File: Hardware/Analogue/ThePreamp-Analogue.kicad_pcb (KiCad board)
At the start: 2 copper layers, 247 x 65 mm, 39 parts, among them IC1 ULN2803CDWR, J1 To preamp, J14 Conn_01x03_Pin, J15 PinSocket10x1, J2 From preamp, J3 Digital In, J4 Digital Pass Through, J5 Power In, J6 Power Out, J7 ADS1115, K1 Input 1, K2 Input 2, K3 Input 3, K4 Input 4, K5 Output Mute, K6 Trigger 1, K7 Trigger 2, K8 Input 5 (opt.), U1 MCP23008-E_SO

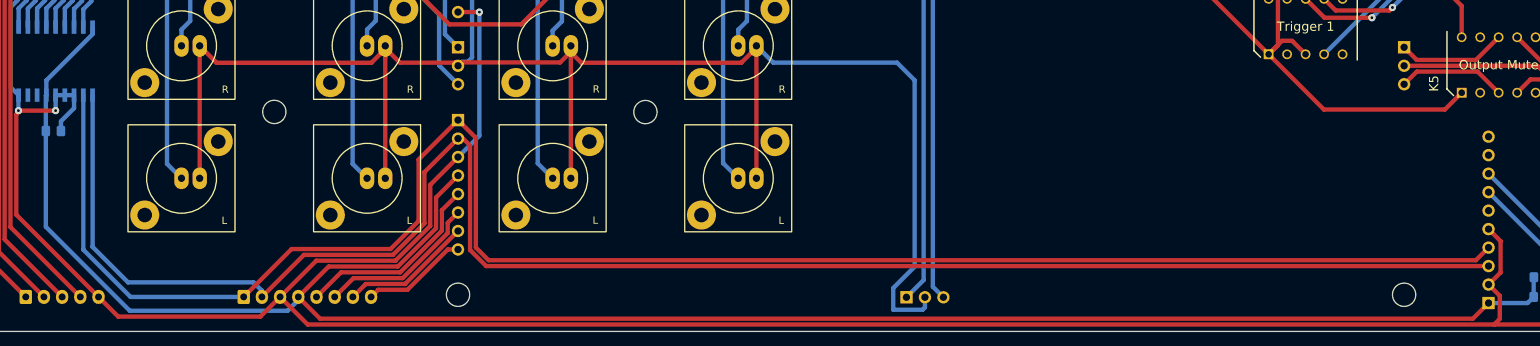
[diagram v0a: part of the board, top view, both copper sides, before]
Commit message: 16 pin IDC connector added for digital control input (GND interleaved)
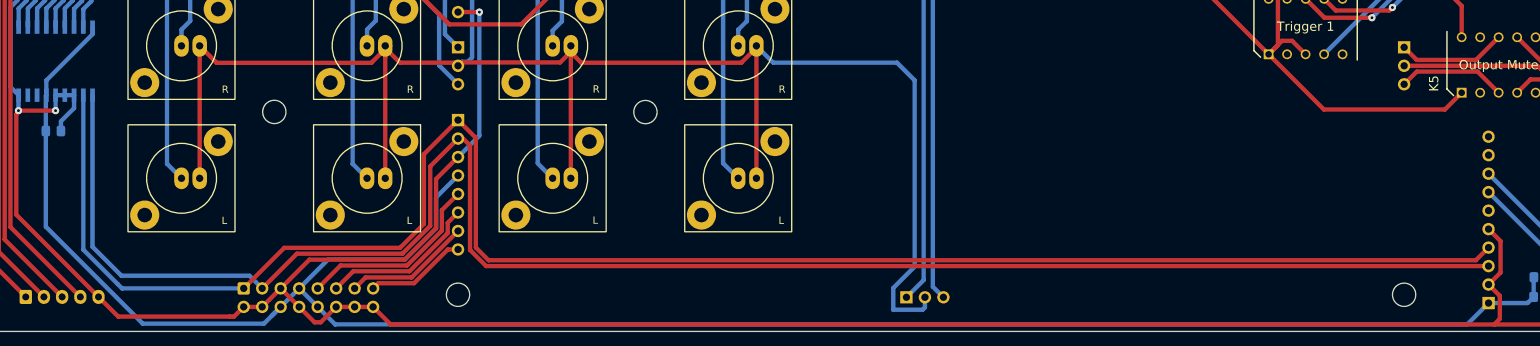
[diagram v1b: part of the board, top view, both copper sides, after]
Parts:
- J15: value PinSocket10x1 -> Switch & trigger outputs and analog inputs
- J3: footprint Connector_JST:JST_XH_B8B-XH-A_1x08_P2.50mm_Vertical -> Connector_IDC:IDC-Header_2x08_P2.54mm_Vertical
- moved J3 1.17 mm to (45.1, 135.9), turned to -90 degrees
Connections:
- J3 pad 2: I2C:SCL -> GND
- J3 pad 3: GND -> I2C:SCL
- J3 pad 4: +3.3V -> GND
- J3 pad 5: SPI:SCK -> GND
- J3 pad 6: SPI:MISO -> +3.3V
- J3 pad 7: SPI:MOSI -> +3.3V
- J3 pad 8: SPI:SS -> GND
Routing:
- net +3.3V: track 277.3 -> 280.9 mm
- net I2C:SCL: track 245.9 -> 243.9 mm
- net GND: track 400.6 -> 402.3 mm
- net SPI:SS: track 14.7 -> 13.9 mm
- net SPI:MOSI: track 18.2 -> 17.5 mm
- net SPI:MISO: track 22.6 -> 21.9 mm
- net SPI:SCK: track 27.0 -> 26.3 mm

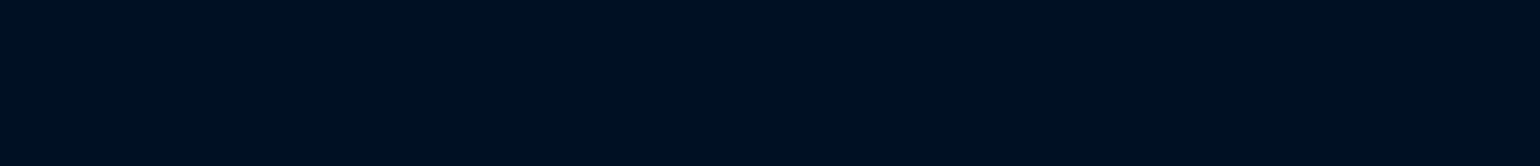
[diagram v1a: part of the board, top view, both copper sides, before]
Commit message: Digital connector (IDC 16) aligned on controller and analog board
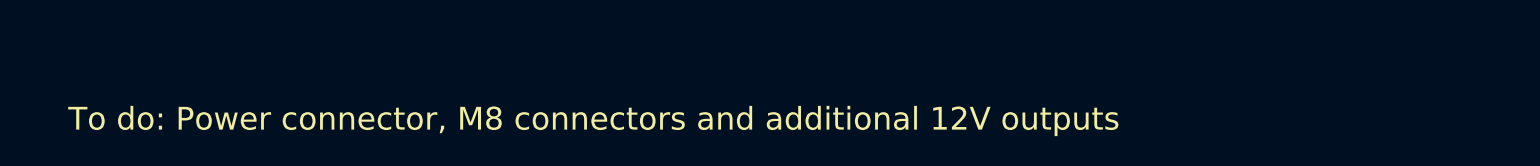
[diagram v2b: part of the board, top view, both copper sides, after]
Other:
- board text added: "To do: Power connector, M8 connectors and additional 12V outputs"
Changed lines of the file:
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@@
     (effects (font (size 1 1) (thickness 0.15)) (justify left bottom mirror))
+  )
+  (gr_text "To do: Power connector, M8 connectors and additional 12V outputs" (at 70.82 153.93) (layer "F.SilkS")
+    (effects (font (size 2 2) (thickness 0.15)) (justify left bottom))
   )
   (gr_text "R" (at 42.11 109.12) (layer "F.SilkS")

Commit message: Added optional M8 connectors for switches, 12V triggers and analog measurements
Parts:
- added J10: Conn_01x04, Connector_M8:M8 4 pin, F.Cu at (268.0, 129.2)
- added J11: Conn_01x03, Connector_M8:M8 3 pin, F.Cu at (285.4, 129.2)
- added J8: Conn_01x04, Connector_M8:M8 4 pin, F.Cu at (267.9, 99.3)
- added J9: Conn_01x03, Connector_M8:M8 3 pin, F.Cu at (285.3, 99.4)
- moved G*** 40.4 mm to (275.8, 87.0)
- moved C1 1.21 mm to (19.0, 113.0)
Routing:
- net GND: track 402.3 -> 481.1 mm
- net Trigger 2 12V out: track 81.5 -> 122.5 mm
- net Trigger 1 12V out: track 70.8 -> 108.1 mm
- net Switch 2 pin 1: track 87.2 -> 115.0 mm
- net Switch 1 pin 1: track 73.1 -> 98.1 mm
- net Switch 2 pin 2: track 88.5 -> 111.2 mm
- net A0: track 71.1 -> 91.9 mm
- net Switch 1 pin 2: track 70.9 -> 91.6 mm
- net A1: track 64.8 -> 84.3 mm
- net +12V: track 300.9 -> 299.5 mm
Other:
- board size 247 x 65 mm -> 285 x 65 mm
- board text added: "To do: Power connector"
- board text added: "v1.1 2024-03"
- board text removed: "To do: Power connector, M8 connectors and additional 12V outputs"
- board text removed: "v1.1 2024-02"

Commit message: Changed power connectors
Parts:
- removed the J5 at (15.2, 137.0)
- removed the REF** at (49.3, 111.6)
- removed the REF** at (100.3, 111.6)
- added J7: Audio Power In, THEPREAMP_POWER_CON:TBP01R2-508-03BK (VERT), B.Cu at (13.0, 137.1)
- added J8: Relay Power In, THEPREAMP_POWER_CON:TBP01R2-508-02BK (VERT), B.Cu at (30.8, 137.1)
- J9: renamed from J7; moved to F.Cu
- moved K8 98.8 mm to (280.8, 120.6), turned to 180 degrees
- moved K7 95.7 mm to (280.8, 90.9), turned to 180 degrees
- moved G*** 50.8 mm to (225.0, 87.4)
- moved C1 11.5 mm to (26.8, 104.6), turned to -90 degrees
- moved J10 6.87 mm to (258.3, 120.5)
- turned J9 to 180 degrees
- renumbered J15 to J10, J8 to J11, J9 to J12, J10 to J13, J11 to J14, J14 to J5, K8 to K2, K2 to K3, K3 to K4, K4 to K5, K5 to K6, K6 to K7, K7 to K8, R3 to R1, R4 to R2, RCA9 to RCA5, RCA5 to RCA6, RCA6 to RCA7, RCA7 to RCA8, RCA8 to RCA9
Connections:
- K7 pad 7: Switch 1 pin 2 -> Switch 1 pin 1
- K7 pad 8: Switch 1 pin 1 -> Switch 1 pin 2
- K8 pad 7: Switch 2 pin 2 -> Switch 2 pin 1
- K8 pad 8: Switch 2 pin 1 -> Switch 2 pin 2
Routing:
- net +12V: track 299.5 -> 466.0 mm, vias 1 -> 3
- net RELAY7: track 173.4 -> 305.8 mm, vias 1 -> 0
- net RELAY6: track 178.8 -> 263.8 mm
- net Trigger 2 12V out: track 122.5 -> 39.9 mm
- net Switch 2 pin 2: track 111.2 -> 30.7 mm
- net Switch 2 pin 1: track 115.0 -> 42.6 mm
- net Switch 1 pin 2: track 91.6 -> 29.2 mm, vias 1 -> 0
- net Trigger 1 12V out: track 108.1 -> 46.7 mm
- net Switch 1 pin 1: track 98.1 -> 38.3 mm, vias 1 -> 0
- net +3.3V: track 280.9 -> 286.6 mm
- net -15V: track 113.1 -> 117.5 mm
- net GND: track 481.1 -> 476.9 mm
- net A0: track 91.9 -> 93.2 mm
- net +15V: track 112.9 -> 112.0 mm
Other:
- board text removed: "G_A"
- board text removed: "To do: Power connector"

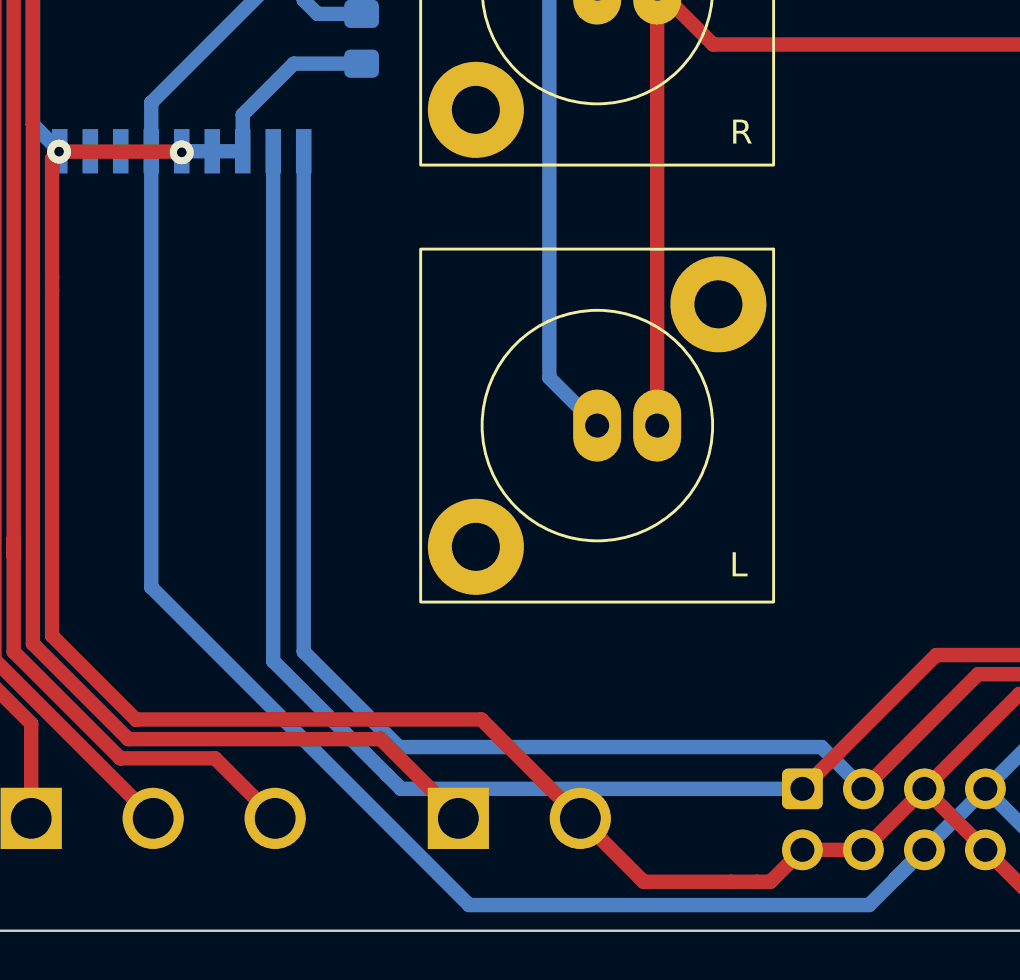
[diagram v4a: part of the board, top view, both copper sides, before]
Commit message: Added 3D-files for connectors
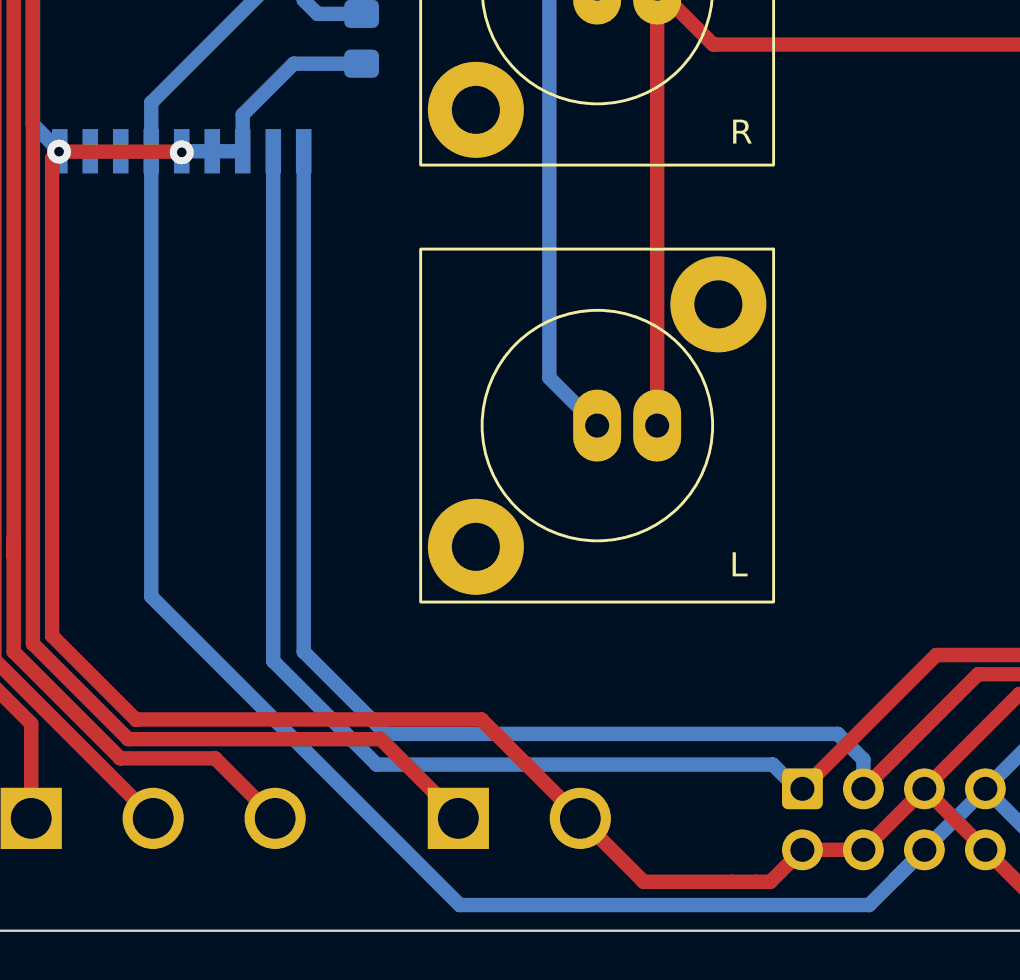
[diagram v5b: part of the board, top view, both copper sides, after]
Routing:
- net I2C:SCL: track 243.9 -> 244.6 mm

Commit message: Ready for production
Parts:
- added J15: Conn_01x02_Pin, Connector_PinHeader_2.54mm:PinHeader_1x02_P2.54mm_Vertical, F.Cu at (224.7, 117.6)
- added R3: 10K, Resistor_SMD:R_0805_2012Metric_Pad1.20x1.40mm_HandSolder, F.Cu at (220.5, 117.6)
- added R4: 10K, Resistor_SMD:R_0805_2012Metric_Pad1.20x1.40mm_HandSolder, F.Cu at (220.5, 115.1)
- J1, J2: footprint Connector_PinHeader_2.54mm:PinHeader_1x03_P2.54mm_Vertical -> Connector_PinSocket_2.54mm:PinSocket_1x03_P2.54mm_Vertical
- J4: footprint Connector_PinHeader_2.54mm:PinHeader_1x08_P2.54mm_Vertical -> Connector_PinSocket_2.54mm:PinSocket_1x08_P2.54mm_Vertical
- J6: footprint Connector_PinHeader_2.54mm:PinHeader_1x05_P2.54mm_Vertical -> Connector_PinSocket_2.54mm:PinSocket_1x05_P2.54mm_Vertical
- R1, R2: moved to F.Cu
- moved R2 17.1 mm to (220.5, 120.2)
- moved R1 12.0 mm to (220.5, 122.7)
- moved G*** 2.31 mm to (224.6, 89.6)
- moved J5 1.56 mm to (136.7, 135.6)
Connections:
- J9 pad 10: unconnected-(J9-Pin_10-Pad10) -> A3
- J9 pad 9: unconnected-(J9-Pin_9-Pad9) -> A2
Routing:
- net +3.3V: track 286.8 -> 301.8 mm, vias 0 -> 4
- net A0: track 93.2 -> 103.1 mm, vias 1 -> 0
- net A2: track 0.00 -> 9.69 mm
- net A3: track 0.00 -> 9.67 mm
- net I2C:SDA: track 249.4 -> 258.1 mm
- net I2C:SCL: track 244.6 -> 253.3 mm
- net GNDA: track 353.3 -> 345.6 mm
- net A1: track 83.9 -> 88.7 mm, vias 0 -> 1
- net Net-(J5-Pin_1): track 45.4 -> 43.7 mm
- net Net-(J5-Pin_3): track 53.1 -> 51.9 mm
- net -15V: track 117.5 -> 116.7 mm
- net RELAY8: track 211.2 -> 210.6 mm
- net +12V: track 466.0 -> 465.5 mm
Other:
- board text added: "2024-03"
- board text added: "3V3"
- board text added: "ANA3 (A2)"
- board text added: "ANA4 (A3)"
- board text added: "Input 5 (Opt.)"
- board text removed: "VDD"
- board text removed: "v1.1 2024-03"
